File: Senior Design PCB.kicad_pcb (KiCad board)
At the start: 2 copper layers, 60 parts, among them J1 Conn_01x02, J2 Conn_01x02, J3 Raspberry_Pi_Zero_2W, J7-1 Conn_01x04, J7-2 Conn_01x04, U1 LM2678SX-5.0/NOPB, U2 MCP3008, U3 MAX38890

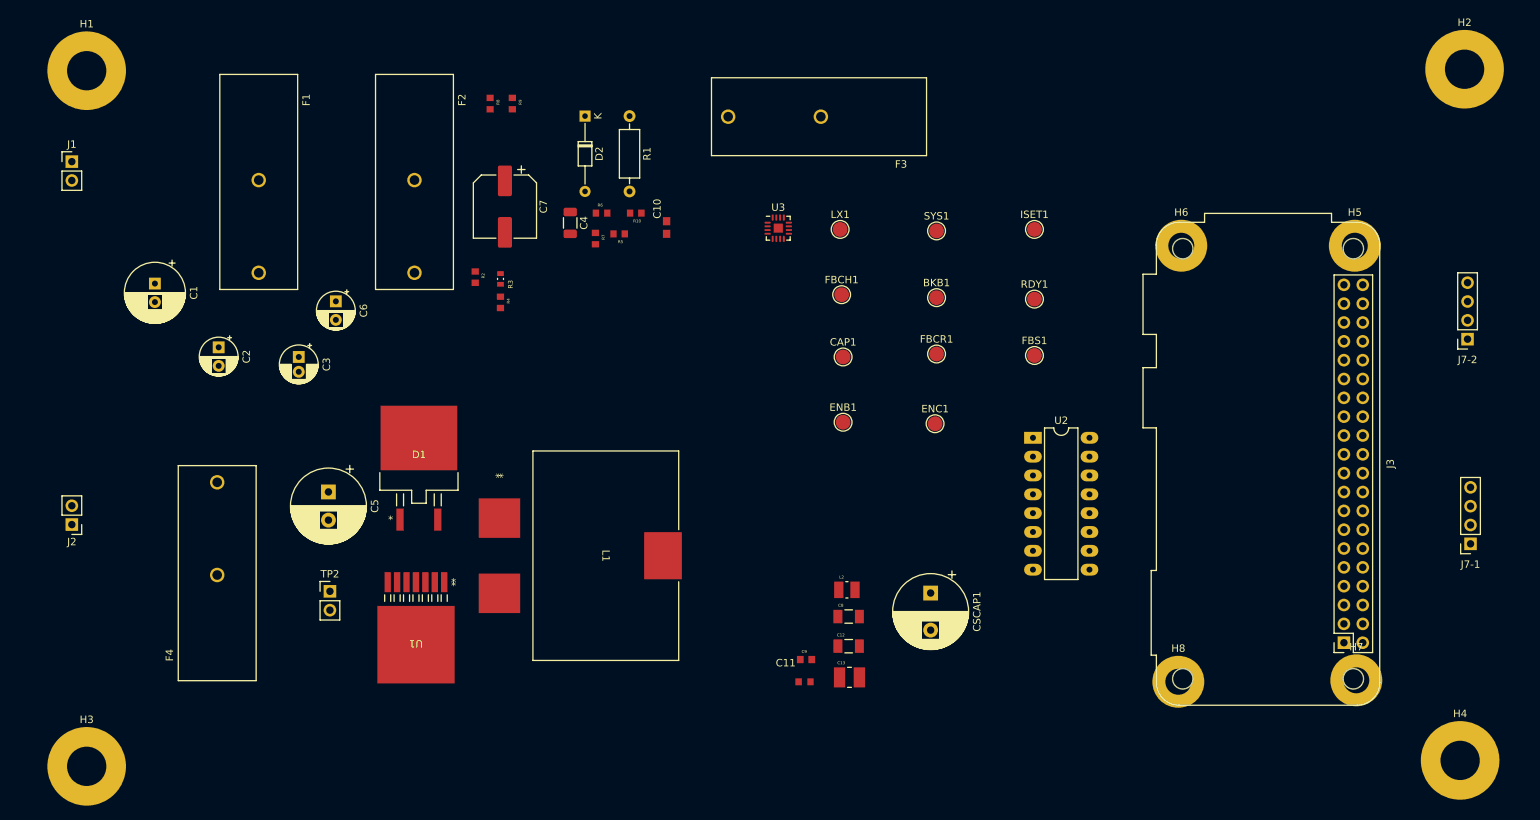
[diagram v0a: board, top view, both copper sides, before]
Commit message: Laid second draft of traces. No ground plane has been added.
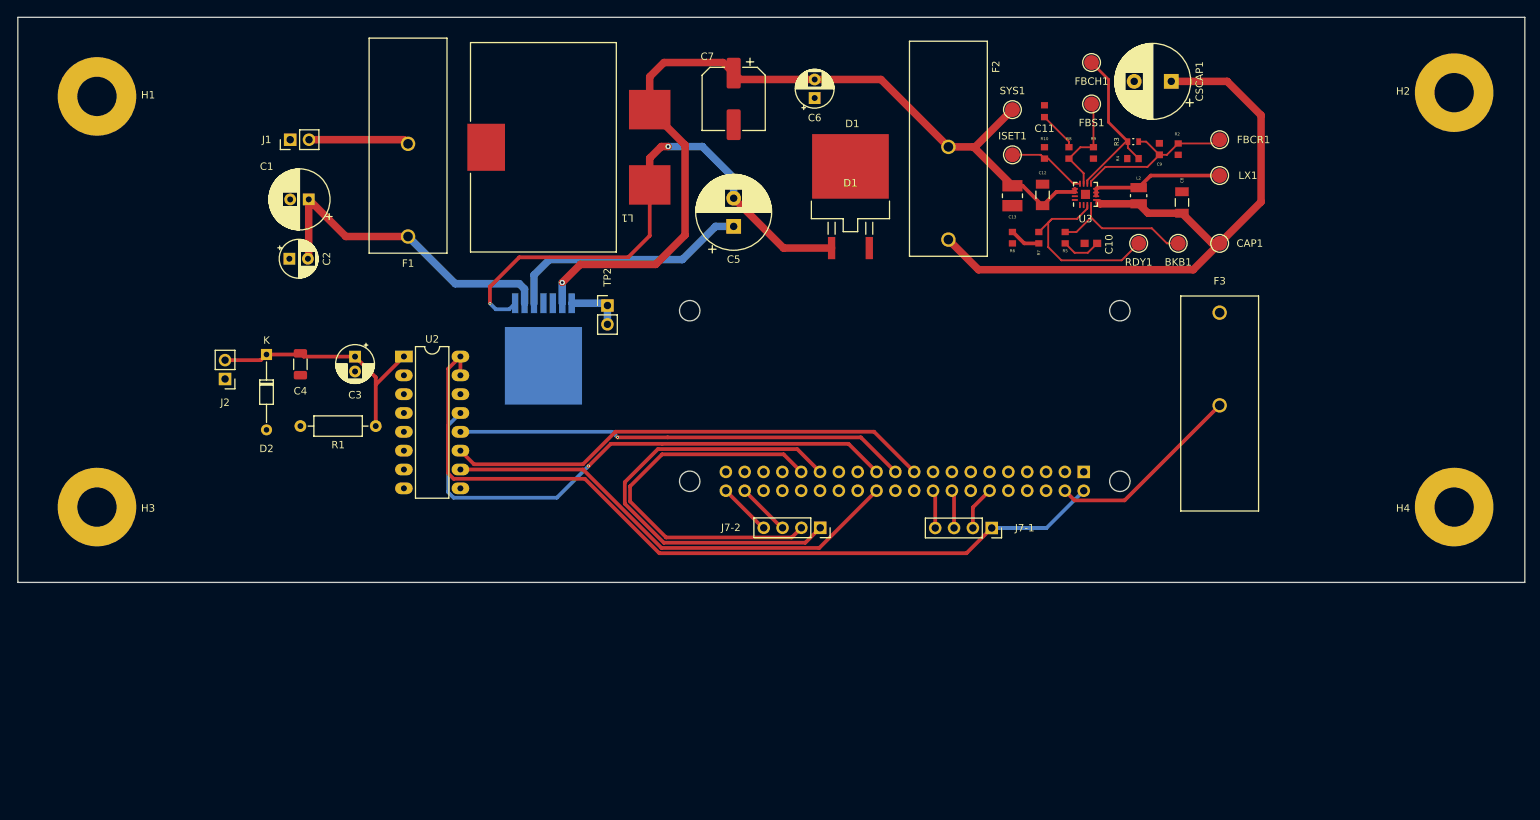
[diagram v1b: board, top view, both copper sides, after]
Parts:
- removed ENB1, ENC1: TestPoint_Small, TestPoint:TestPoint_Pad_D2.0mm
- removed F4: Fuse, AAA_senior_design:FUSE_4525
- removed H5, H6, H7, H8: MountingHole_Pad, MountingHole:MountingHole_3.5mm_Pad
- J3, U1: moved to B.Cu
- moved R2 96.3 mm to (202.2, 68.6), turned to 90 degrees
- moved J7-2 90.9 mm to (153.9, 119.6), turned to -90 degrees
- moved R4 87.5 mm to (196.1, 69.8), turned to 180 degrees
- moved R3 87.3 mm to (196.1, 67.6), turned to 180 degrees
- moved U2 85.5 mm to (97.8, 96.5)
- moved C9 83.7 mm to (199.6, 68.6), turned to 90 degrees
- moved C11 83.5 mm to (184.2, 63.5), turned to 90 degrees
- moved R9 78.6 mm to (190.8, 69.1)
- moved R8 78.3 mm to (187.5, 69.1)
- moved CSCAP1 76.2 mm to (201.2, 59.4), turned to 180 degrees
- moved F2 72.1 mm to (171.2, 68.5)
- moved C8 71.7 mm to (202.7, 75.8), turned to 90 degrees
- moved C6 70.1 mm to (153.2, 61.7), turned to 90 degrees
- moved D1 68.8 mm to (158.0, 73.2)
- moved C13 68.6 mm to (179.8, 74.9), turned to -90 degrees
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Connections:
- J2 pad 2: Net-(J2-Pin_2) -> /Vsig
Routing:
- net /5V: track 0.00 -> 129.6 mm, vias 0 -> 1
- net Net-(J7-1-Pin_1): track 0.00 -> 112.6 mm
- net Net-(U3-CAP): track 0.00 -> 91.9 mm
- net Net-(J3-GPIO11): track 0.00 -> 74.1 mm, vias 0 -> 1
- net Net-(D1-K): track 0.00 -> 73.6 mm, vias 0 -> 2
- net Net-(J3-GPIO10): track 0.00 -> 66.0 mm
- net Net-(J3-GPIO8): track 0.00 -> 63.7 mm
- net Net-(J3-KEY1): track 0.00 -> 61.7 mm
- net Net-(J3-GPIO9): track 0.00 -> 60.9 mm, vias 0 -> 1
- net Net-(J3-KEY0): track 0.00 -> 53.5 mm
- net /12V: track 0.00 -> 44.2 mm
- net /Vsig: track 0.00 -> 34.0 mm
- net Net-(U1-CB): track 0.00 -> 33.4 mm
- net Net-(F3-Pad1): track 0.00 -> 26.7 mm
- net Net-(U3-RDY): track 0.00 -> 26.2 mm
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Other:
- board outline added: 203.2 x 76.2 mm

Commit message: Laid fourth draft of traces and passed all drc checks. gnd planes added and the mounting holes are added, as well. Remaining steps are to add leds or 50k ohm resistor.
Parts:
- removed F2, F3: Fuse, AAA_senior_design:FUSE_4525
- added H10: MountingHole_Pad, MountingHole:MountingHole_3.2mm_M3_Pad, F.Cu at (168.9, 78.7)
- added H11: MountingHole_Pad, MountingHole:MountingHole_3.2mm_M3_Pad, F.Cu at (90.5, 115.2)
- added H12: MountingHole_Pad, MountingHole:MountingHole_3.2mm_M3_Pad, F.Cu at (205.5, 115.3)
- added H13: MountingHole_Pad, MountingHole:MountingHole_3.2mm_M3_Pad, F.Cu at (94.5, 62.6)
- added H14: MountingHole_Pad, MountingHole:MountingHole_3.2mm_M3_Pad, F.Cu at (172.1, 62.7)
- added H5: MountingHole_Pad, MountingHole:MountingHole_3.2mm_M3_Pad, F.Cu at (236.9, 62.6)
- added H6: MountingHole_Pad, MountingHole:MountingHole_3.2mm_M3_Pad, F.Cu at (236.9, 80.1)
- added H7: MountingHole_Pad, MountingHole:MountingHole_3.2mm_M3_Pad, F.Cu at (236.9, 97.8)
- added H8: MountingHole_Pad, MountingHole:MountingHole_3.2mm_M3_Pad, F.Cu at (236.9, 115.2)
- added H9: MountingHole_Pad, MountingHole:MountingHole_3.2mm_M3_Pad, F.Cu at (126.5, 101.1)
- H1, H2, H3, H4: footprint MountingHole:MountingHole_5.3mm_M5_Pad -> MountingHole:MountingHole_3.2mm_M3_Pad
- moved H2 183.1 mm to (57.3, 80.1)
- moved H4 182.1 mm to (57.3, 115.2)
- moved H3 19.1 mm to (57.3, 97.8)
- moved F1 13.6 mm to (84.8, 68.5)
- moved C1 11.5 mm to (73.5, 75.4)
- moved C2 11.5 mm to (70.9, 83.4)
- moved J1 11.5 mm to (71.0, 67.3)
- moved RDY1 9.91 mm to (186.9, 81.3)
- moved R5 8.92 mm to (195.8, 81.3), turned to 180 degrees
- moved L1 7.42 mm to (109.2, 68.3)
- moved D1 7.15 mm to (153.9, 67.3)
- moved FBCH1 6.63 mm to (192.8, 63.1)
- moved C6 6.50 mm to (153.4, 55.2), turned to -90 degrees
- moved CSCAP1 5.13 mm to (206.4, 59.4)
- moved FBS1 2.71 mm to (187.8, 63.0)
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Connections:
- C8 pad 1: Net-(U3-CAP) -> /5V
- CAP1 pad 1: Net-(U3-CAP) -> /5V
- CSCAP1 pad 1: Net-(U3-CAP) -> /5V
- D1 pad 3: (no net) -> GND
- J3 pad 4: Net-(F3-Pad1) -> /5V
- L1 pad 3: (no net) -> GND
- L2 pad 1: Net-(U3-CAP) -> /5V
- R2 pad 1: Net-(U3-CAP) -> /5V
- U3 pad 17: (no net) -> GND
- U3 pad 5: Net-(U3-CAP) -> /5V
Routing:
- net /5V: track 129.6 -> 260.5 mm, vias 1 -> 3
- net Net-(U3-CAP): track 91.9 -> 0.00 mm
- net Net-(J3-GPIO2): track 5.37 -> 48.1 mm, vias 0 -> 1
- net Net-(F3-Pad1): track 26.7 -> 0.00 mm
- net Net-(U3-RDY): track 26.2 -> 12.5 mm
- net /12V: track 44.2 -> 55.7 mm
- net Net-(U3-FBCH): track 23.7 -> 16.5 mm
- net Net-(D1-K): track 73.6 -> 69.7 mm
- net Net-(U3-BKB): track 19.2 -> 22.1 mm
- net GND: track 0.00 -> 2.75 mm, vias 0 -> 5
- net Net-(J3-GPIO8): track 63.7 -> 65.7 mm
- net Net-(J1-Pin_2): track 13.6 -> 11.7 mm
- net Net-(J7-1-Pin_1): track 112.6 -> 114.4 mm
- net Net-(J3-GPIO10): track 66.0 -> 64.5 mm
- net Net-(U3-FBS): track 14.1 -> 14.7 mm
- added copper zone on B.Cu, net GND
- added copper zone on F.Cu, net GND

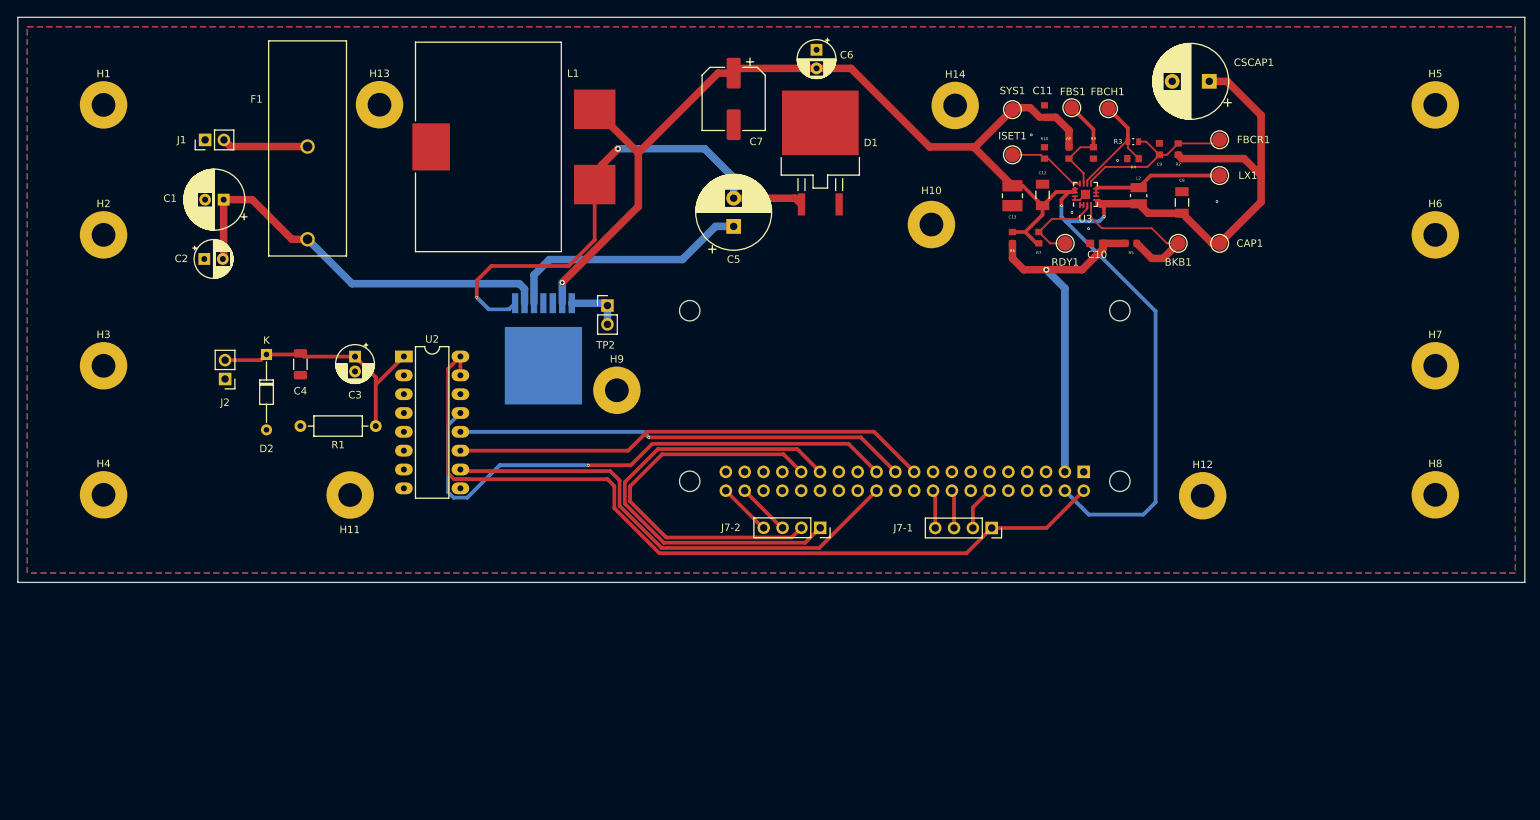
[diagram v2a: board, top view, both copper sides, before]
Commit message: Mark Bruno edits implemented.
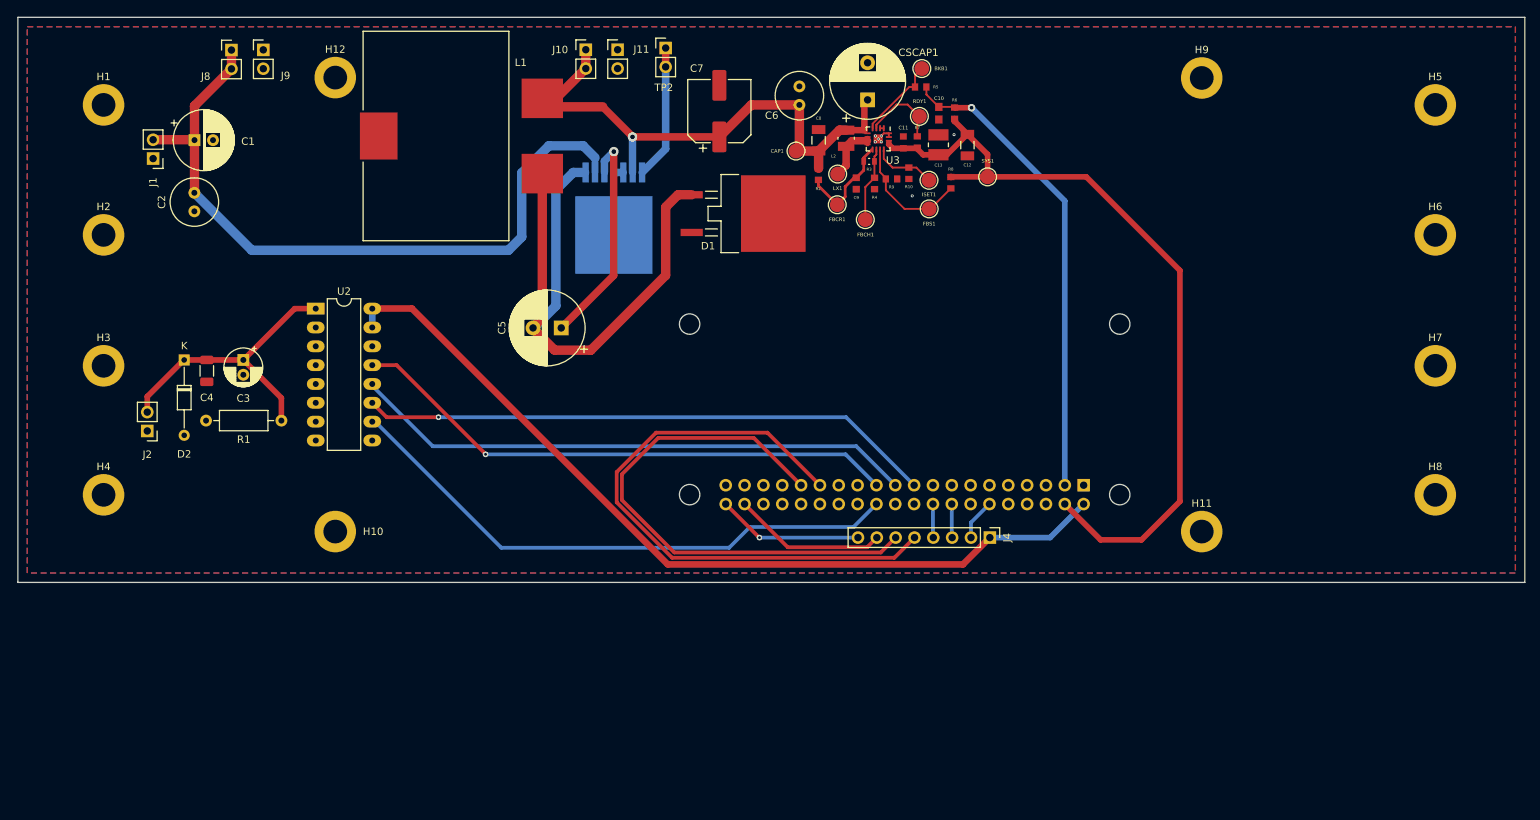
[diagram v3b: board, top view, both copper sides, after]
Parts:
- removed F1: Fuse, AAA_senior_design:FUSE_4525
- removed H14: MountingHole_Pad, MountingHole:MountingHole_3.2mm_M3_Pad
- removed the H9 at (126.5, 101.1)
- removed J7-1, J7-2: Conn_01x04, Connector_PinSocket_2.54mm:PinSocket_1x04_P2.54mm_Vertical
- added J10: Conn_01x02, Connector_PinHeader_2.54mm:PinHeader_1x02_P2.54mm_Vertical, F.Cu at (122.3, 55.2)
- added J11: Conn_01x02, Connector_PinHeader_2.54mm:PinHeader_1x02_P2.54mm_Vertical, F.Cu at (126.6, 55.2)
- added J4: Conn_01x08, Connector_PinHeader_2.54mm:PinHeader_1x08_P2.54mm_Vertical, F.Cu at (176.8, 121.0)
- added J8: Conn_01x02, Connector_PinHeader_2.54mm:PinHeader_1x02_P2.54mm_Vertical, F.Cu at (74.5, 55.2)
- added J9: Conn_01x02, Connector_PinHeader_2.54mm:PinHeader_1x02_P2.54mm_Vertical, F.Cu at (78.8, 55.2)
- C2, C6: footprint Capacitor_THT:CP_Radial_D5.0mm_P2.50mm -> Capacitor_THT:C_Radial_D6.3mm_H11.0mm_P2.50mm
- H1, H2, H3, H4, H5, H6, H7, H8: footprint MountingHole:MountingHole_3.2mm_M3_Pad -> MountingHole:MountingHole_3.2mm_M3_DIN965_Pad
- H10: renamed from H11; footprint MountingHole:MountingHole_3.2mm_M3_Pad -> MountingHole:MountingHole_3.2mm_M3_DIN965_Pad
- H11: renamed from H12; footprint MountingHole:MountingHole_3.2mm_M3_Pad -> MountingHole:MountingHole_3.2mm_M3_DIN965_Pad
- H12: renamed from H13; footprint MountingHole:MountingHole_3.2mm_M3_Pad -> MountingHole:MountingHole_3.2mm_M3_DIN965_Pad
- H9: renamed from H10; footprint MountingHole:MountingHole_3.2mm_M3_Pad -> MountingHole:MountingHole_3.2mm_M3_DIN965_Pad
- moved CAP1 58.5 mm to (150.6, 68.8)
- moved FBCR1 52.3 mm to (156.2, 76.1)
- moved LX1 51.5 mm to (156.3, 71.9)
- moved C8 49.7 mm to (153.7, 67.4)
- moved R2 48.6 mm to (153.7, 72.0), turned to -90 degrees
- moved CSCAP1 46.1 mm to (160.3, 61.9), turned to 90 degrees
- moved BKB1 41.8 mm to (167.6, 57.7)
- moved H9 41.5 mm to (205.4, 59.0)
- moved C9 41.1 mm to (158.8, 73.2), turned to -90 degrees
- moved L2 40.2 mm to (157.4, 67.1), turned to -90 degrees
- moved FBCH1 36.0 mm to (160.0, 78.1)
- moved R3 35.7 mm to (160.5, 70.2), turned to 0 degrees
- moved TP2 35.6 mm to (133.1, 54.9)
- moved R5 35.3 mm to (167.5, 60.2), turned to 0 degrees
- moved R4 35.0 mm to (161.2, 73.2), turned to -90 degrees
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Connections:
- C6 pad 2: /5V -> /5V - unreg
- C7 pad 1: /5V -> /5V - unreg
- C8 pad 1: /5V -> /5V - unreg
- CAP1 pad 1: /5V -> /5V - unreg
- CSCAP1 pad 1: /5V -> /5V - unreg
- J1 pad 2: Net-(J1-Pin_2) -> /12V
- L1 pad 2: /5V -> /5V - unreg
- L2 pad 1: /5V -> /5V - unreg
- R2 pad 1: /5V -> /5V - unreg
- U1 pad 6: /5V -> /5V - unreg
- U3 pad 5: /5V -> /5V - unreg
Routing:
- net /5V: track 260.5 -> 109.1 mm, vias 3 -> 0
- net /5V - unreg: track 0.00 -> 76.3 mm, vias 0 -> 1
- net /12V: track 55.7 -> 97.8 mm
- net Net-(J3-KEY0): track 53.5 -> 73.0 mm
- net Net-(J3-KEY1): track 61.7 -> 81.0 mm
- net Net-(J3-GPIO2): track 48.1 -> 63.9 mm
- net Net-(J3-GPIO9): track 60.9 -> 76.4 mm, vias 1 -> 0
- net Net-(D1-K): track 69.7 -> 83.3 mm, vias 2 -> 0
- net Net-(J3-MOSI1): track 7.18 -> 20.8 mm
- net Net-(J3-GPIO10): track 64.5 -> 77.7 mm, vias 0 -> 1
- net Net-(J3-SCLK1): track 7.18 -> 19.7 mm, vias 0 -> 1
- net Net-(J3-GPIO8): track 65.7 -> 77.5 mm
- net Net-(J1-Pin_2): track 11.7 -> 0.00 mm
- net Net-(U3-BKB): track 22.1 -> 11.2 mm
- net Net-(TP2-Pin_1): track 7.49 -> 18.1 mm
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
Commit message: Final files added to 'most recent files' branch.
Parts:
- moved C4 9.63 mm to (70.8, 108.1)
- moved R4 9.63 mm to (160.9, 82.8)
- moved R9 9.63 mm to (163.2, 82.2)
- moved BKB1 9.63 mm to (167.3, 67.3)
- moved C12 9.63 mm to (173.4, 77.6)
- moved C9 9.63 mm to (158.4, 82.8)
- moved FBCR1 9.63 mm to (155.9, 85.7)
- moved H4 9.63 mm to (56.9, 124.8)
- moved H8 9.63 mm to (236.5, 124.8)
- moved J1 9.63 mm to (63.6, 79.5)
- moved R1 9.63 mm to (80.9, 114.8)
- moved R10 9.63 mm to (165.5, 81.5)
- moved R3 9.63 mm to (160.1, 79.9)
- moved RDY1 9.63 mm to (166.9, 73.8)
- moved U1 9.63 mm to (125.7, 89.6)
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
